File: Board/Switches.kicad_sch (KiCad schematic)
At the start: 128 parts, among them SW10 SW_Push_45deg, SW11 SW_Push_45deg, SW12 SW_Push_45deg, SW13 SW_Push_45deg, SW14 SW_Push_45deg, SW15 SW_Push_45deg, SW16 SW_Push_45deg, SW17 SW_Push_45deg, SW18 SW_Push_45deg, SW19 SW_Push_45deg, SW2 SW_Push_45deg, SW20 SW_Push_45deg, SW21 SW_Push_45deg, SW22 SW_Push_45deg, SW23 SW_Push_45deg, SW24 SW_Push_45deg, SW25 SW_Push_45deg, SW26 SW_Push_45deg, SW27 SW_Push_45deg, SW28 SW_Push_45deg, SW29 SW_Push_45deg, SW3 SW_Push_45deg, SW30 SW_Push_45deg, SW31 SW_Push_45deg, SW32 SW_Push_45deg, SW33 SW_Push_45deg, SW34 SW_Push_45deg, SW35 SW_Push_45deg, SW36 SW_Push_45deg, SW37 SW_Push_45deg, SW38 SW_Push_45deg, SW39 SW_Push_45deg, SW4 SW_Push_45deg, SW40 SW_Push_45deg, SW41 SW_Push_45deg, SW42 SW_Push_45deg, SW43 SW_Push_45deg, SW44 SW_Push_45deg, SW45 SW_Push_45deg, SW46 SW_Push_45deg, SW47 SW_Push_45deg, SW48 SW_Push_45deg, SW49 SW_Push_45deg, SW5 SW_Push_45deg, SW50 SW_Push_45deg, SW51 SW_Push_45deg, SW52 SW_Push_45deg, SW53 SW_Push_45deg, SW54 SW_Push_45deg, SW55 SW_Push_45deg, SW56 SW_Push_45deg, SW57 SW_Push_45deg, SW58 SW_Push_45deg, SW59 SW_Push_45deg, SW6 SW_Push_45deg, SW60 SW_Push_45deg, SW61 SW_Push_45deg, SW62 SW_Push_45deg, SW63_BL1 SW_Push_45deg, SW64_NONE1 SW_Push_45deg, SW65_NONE1 SW_Push_45deg, SW7 SW_Push_45deg, SW8 SW_Push_45deg, SW9 SW_Push_45deg

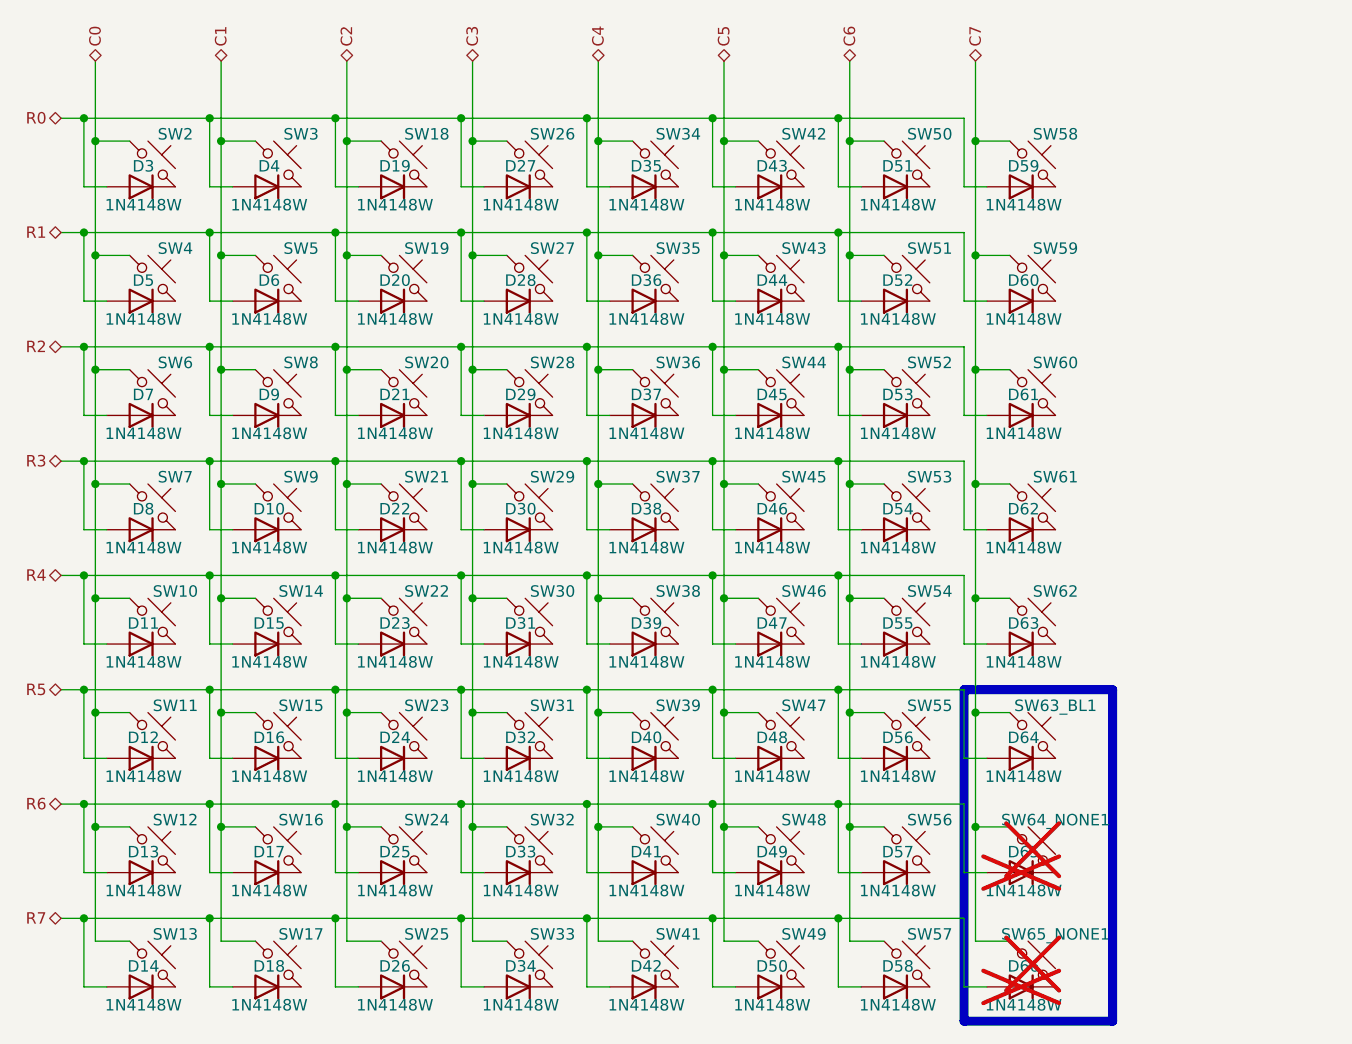
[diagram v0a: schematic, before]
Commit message: Uprava pro jednodusi kontrolu
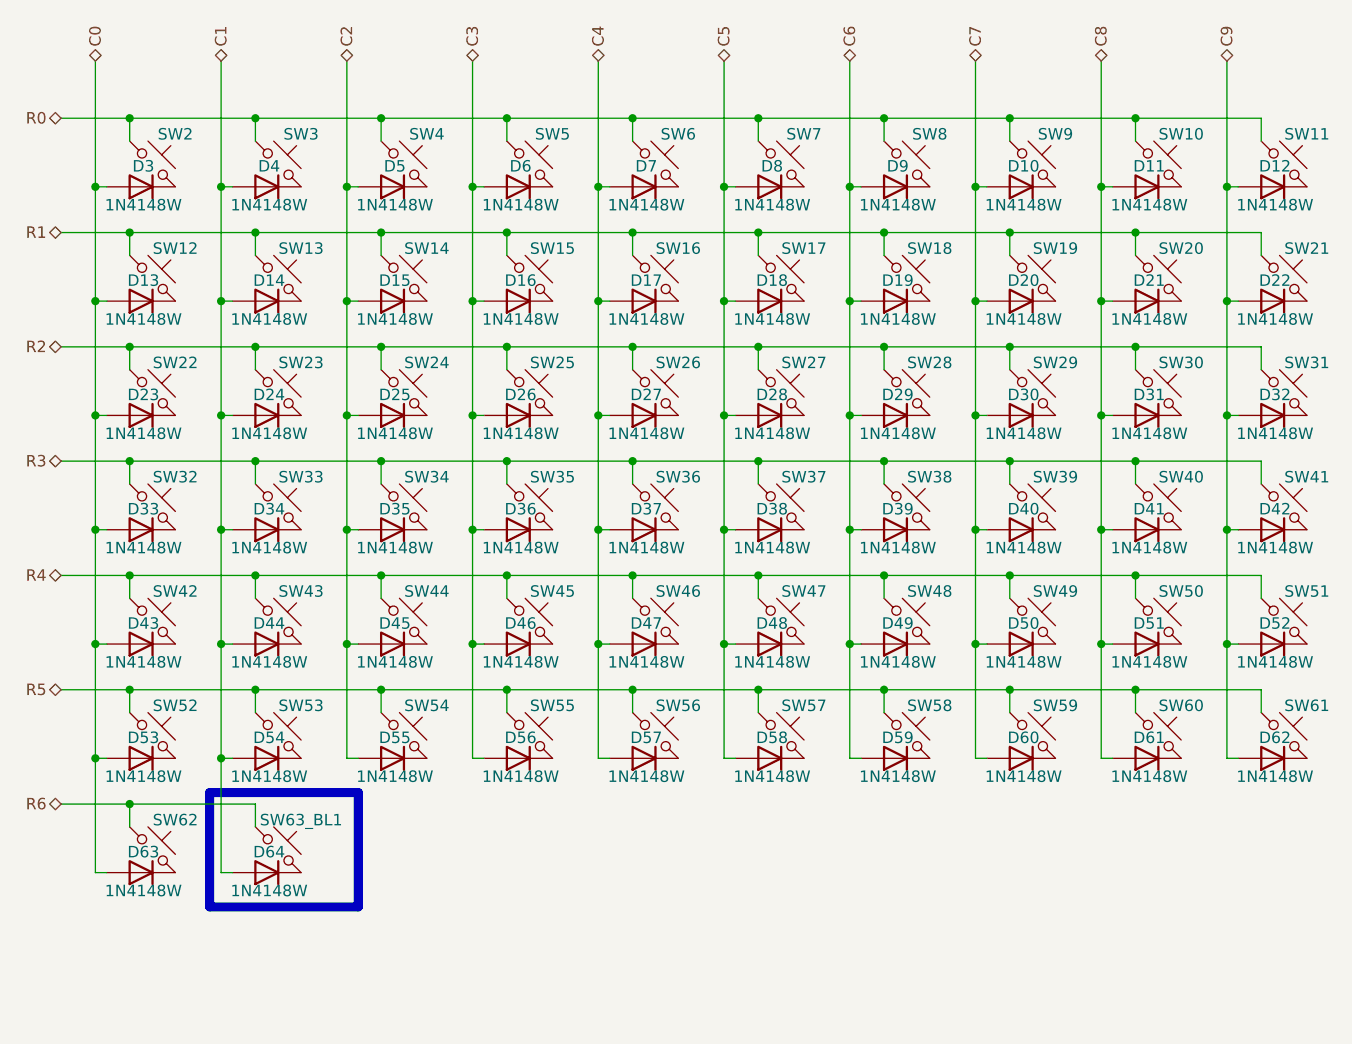
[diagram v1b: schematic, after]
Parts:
- removed D65, D66: 1N4148W, symbol Device:D
- removed SW64_NONE1, SW65_NONE1: SW_Push_45deg, Button_Switch_Keyboard:SW_Cherry_MX_1.00u_PCB, symbol Switch:SW_Push_45deg
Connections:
- net C0: now also D13.2 (A), D23.2 (A), D3.2 (A), D33.2 (A), D43.2 (A), D53.2 (A), D63.2 (A); no longer SW10.1, SW11.1, SW12.1, SW13.1, SW2.1, SW4.1, SW6.1, SW7.1
- net C1: now also D14.2 (A), D24.2 (A), D34.2 (A), D4.2 (A), D44.2 (A), D54.2 (A), D64.2 (A); no longer SW14.1, SW15.1, SW16.1, SW17.1, SW3.1, SW5.1, SW8.1, SW9.1
- net C2: now also D15.2 (A), D25.2 (A), D35.2 (A), D45.2 (A), D5.2 (A), D55.2 (A); no longer SW18.1, SW19.1, SW20.1, SW21.1, SW22.1, SW23.1, SW24.1, SW25.1
- net C3: now also D16.2 (A), D26.2 (A), D36.2 (A), D46.2 (A), D56.2 (A), D6.2 (A); no longer SW26.1, SW27.1, SW28.1, SW29.1, SW30.1, SW31.1, SW32.1, SW33.1
- net C4: now also D17.2 (A), D27.2 (A), D37.2 (A), D47.2 (A), D57.2 (A), D7.2 (A); no longer SW34.1, SW35.1, SW36.1, SW37.1, SW38.1, SW39.1, SW40.1, SW41.1
- net C5: now also D18.2 (A), D28.2 (A), D38.2 (A), D48.2 (A), D58.2 (A), D8.2 (A); no longer SW42.1, SW43.1, SW44.1, SW45.1, SW46.1, SW47.1, SW48.1, SW49.1
- net C6: now also D19.2 (A), D29.2 (A), D39.2 (A), D49.2 (A), D59.2 (A), D9.2 (A); no longer SW50.1, SW51.1, SW52.1, SW53.1, SW54.1, SW55.1, SW56.1, SW57.1
- net C7: now also D10.2 (A), D20.2 (A), D30.2 (A), D40.2 (A), D50.2 (A), D60.2 (A); no longer SW58.1, SW59.1, SW60.1, SW61.1, SW62.1, SW63_BL1.1
- net R0: now also SW10.1, SW11.1, SW2.1, SW3.1, SW4.1, SW5.1, SW6.1, SW7.1, SW8.1, SW9.1; no longer D19.2 (A), D27.2 (A), D3.2 (A), D35.2 (A), D4.2 (A), D43.2 (A), D51.2 (A), D59.2 (A)
- net R1: now also SW12.1, SW13.1, SW14.1, SW15.1, SW16.1, SW17.1, SW18.1, SW19.1, SW20.1, SW21.1; no longer D20.2 (A), D28.2 (A), D36.2 (A), D44.2 (A), D5.2 (A), D52.2 (A), D6.2 (A), D60.2 (A)
- net R2: now also SW22.1, SW23.1, SW24.1, SW25.1, SW26.1, SW27.1, SW28.1, SW29.1, SW30.1, SW31.1; no longer D21.2 (A), D29.2 (A), D37.2 (A), D45.2 (A), D53.2 (A), D61.2 (A), D7.2 (A), D9.2 (A)
- net R3: now also SW32.1, SW33.1, SW34.1, SW35.1, SW36.1, SW37.1, SW38.1, SW39.1, SW40.1, SW41.1; no longer D10.2 (A), D22.2 (A), D30.2 (A), D38.2 (A), D46.2 (A), D54.2 (A), D62.2 (A), D8.2 (A)
- net R4: now also SW42.1, SW43.1, SW44.1, SW45.1, SW46.1, SW47.1, SW48.1, SW49.1, SW50.1, SW51.1; no longer D11.2 (A), D15.2 (A), D23.2 (A), D31.2 (A), D39.2 (A), D47.2 (A), D55.2 (A), D63.2 (A)
- net R5: now also SW52.1, SW53.1, SW54.1, SW55.1, SW56.1, SW57.1, SW58.1, SW59.1, SW60.1, SW61.1; no longer D12.2 (A), D16.2 (A), D24.2 (A), D32.2 (A), D40.2 (A), D48.2 (A), D56.2 (A), D64.2 (A)
- net R6: now also SW62.1, SW63_BL1.1; no longer D13.2 (A), D17.2 (A), D25.2 (A), D33.2 (A), D41.2 (A), D49.2 (A), D57.2 (A)
- removed net R7: D14.2 (A), D18.2 (A), D26.2 (A), D34.2 (A), D42.2 (A), D50.2 (A), D58.2 (A)
- new net C8: D11.2 (A), D21.2 (A), D31.2 (A), D41.2 (A), D51.2 (A), D61.2 (A)
- new net C9: D12.2 (A), D22.2 (A), D32.2 (A), D42.2 (A), D52.2 (A), D62.2 (A)
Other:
- moved on the sheet: D64, SW63_BL1
